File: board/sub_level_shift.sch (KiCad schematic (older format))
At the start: 31 parts, among them Q1401 Q_NPN_BEC, Q1402 Q_NPN_BEC, Q1403 Q_NPN_BEC, U1401 74LVC4245A, U1402 74LVC4245A, U1403 74LVC4245A, U1404 74LVC4245A, U1405 74LVC4245A, U1406 74LVC4245A, U1407 74LVC4245A

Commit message: Most footprints associated
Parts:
- C1401, C1402, C1403, C1404, C1405, C1406, C1407, C1408, C1409, C1410, C1411, C1412, C1413, C1414: footprint (none) -> Capacitor_SMD:C_0603_1608Metric
- Q1401, Q1402, Q1403: footprint (none) -> Package_TO_SOT_SMD:SOT-23
- R1401, R1402, R1403, R1404, R1405, R1406, R1407: footprint (none) -> Resistor_SMD:R_0603_1608Metric
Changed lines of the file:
@@
 F 0 "R1404" V 7418 4750 50  0000 C CNN
 F 1 "1k" V 7509 4750 50  0000 C CNN
-F 2 "" V 7555 4750 50  0001 C CNN
+F 2 "Resistor_SMD:R_0603_1608Metric" V 7555 4750 50  0001 C CNN
 F 3 "~" H 7625 4750 50  0001 C CNN
 	1    7625 4750
@@
 F 0 "Q1402" H 7466 4750 50  0000 L CNN
 F 1 "Q_NPN_BEC" H 7466 4705 50  0001 L CNN
-F 2 "" H 7475 4850 50  0001 C CNN
+F 2 "Package_TO_SOT_SMD:SOT-23" H 7475 4850 50  0001 C CNN
 F 3 "~" H 7275 4750 50  0001 C CNN
 	1    7275 4750
@@
 F 0 "R1403" H 6875 4350 50  0000 L CNN
 F 1 "4K7" H 6950 4250 50  0000 L CNN
-F 2 "" V 7105 4300 50  0001 C CNN
+F 2 "Resistor_SMD:R_0603_1608Metric" V 7105 4300 50  0001 C CNN
 F 3 "~" H 7175 4300 50  0001 C CNN
 	1    7175 4300
@@
 F 0 "R1407" H 6250 5900 50  0000 L CNN
 F 1 "4K7" H 6325 5800 50  0000 L CNN
-F 2 "" V 6480 5850 50  0001 C CNN
+F 2 "Resistor_SMD:R_0603_1608Metric" V 6480 5850 50  0001 C CNN
 F 3 "~" H 6550 5850 50  0001 C CNN
 	1    6550 5850
@@
 F 0 "R1402" V 8293 3775 50  0000 C CNN
 F 1 "1k" V 8384 3775 50  0000 C CNN
-F 2 "" V 8430 3775 50  0001 C CNN
+F 2 "Resistor_SMD:R_0603_1608Metric" V 8430 3775 50  0001 C CNN
 F 3 "~" H 8500 3775 50  0001 C CNN
 	1    8500 3775
@@
 F 0 "Q1401" H 8341 3775 50  0000 L CNN
 F 1 "Q_NPN_BEC" H 8341 3730 50  0001 L CNN
-F 2 "" H 8350 3875 50  0001 C CNN
+F 2 "Package_TO_SOT_SMD:SOT-23" H 8350 3875 50  0001 C CNN
 F 3 "~" H 8150 3775 50  0001 C CNN
 	1    8150 3775
@@
 F 0 "R1401" H 7750 3375 50  0000 L CNN
 F 1 "4K7" H 7825 3275 50  0000 L CNN
-F 2 "" V 7980 3325 50  0001 C CNN
+F 2 "Resistor_SMD:R_0603_1608Metric" V 7980 3325 50  0001 C CNN
 F 3 "~" H 8050 3325 50  0001 C CNN
 	1    8050 3325
@@
 F 0 "Q1403" H 8516 5550 50  0000 L CNN
 F 1 "Q_NPN_BEC" H 8516 5505 50  0001 L CNN
-F 2 "" H 8525 5650 50  0001 C CNN
+F 2 "Package_TO_SOT_SMD:SOT-23" H 8525 5650 50  0001 C CNN
 F 3 "~" H 8325 5550 50  0001 C CNN
 	1    8325 5550
@@
 F 0 "R1405" H 8500 5150 50  0000 L CNN
 F 1 "4K7" H 8500 5050 50  0000 L CNN
-F 2 "" V 8355 5100 50  0001 C CNN
+F 2 "Resistor_SMD:R_0603_1608Metric" V 8355 5100 50  0001 C CNN
 F 3 "~" H 8425 5100 50  0001 C CNN
 	1    8425 5100
@@
 F 0 "R1406" V 7775 5425 50  0000 L CNN
 F 1 "4K7" V 7875 5475 50  0000 L CNN
-F 2 "" V 7905 5550 50  0001 C CNN
+F 2 "Resistor_SMD:R_0603_1608Metric" V 7905 5550 50  0001 C CNN
 F 3 "~" H 7975 5550 50  0001 C CNN
 	1    7975 5550
@@
 F 0 "C1404" H 9715 2021 50  0000 L CNN
 F 1 "1u" H 9715 1930 50  0000 L CNN
-F 2 "" H 9638 1825 50  0001 C CNN
+F 2 "Capacitor_SMD:C_0603_1608Metric" H 9638 1825 50  0001 C CNN
 F 3 "~" H 9600 1975 50  0001 C CNN
 	1    9600 1975
@@
 F 0 "C1405" H 10190 2021 50  0000 L CNN
 F 1 "1u" H 10190 1930 50  0000 L CNN
-F 2 "" H 10113 1825 50  0001 C CNN
+F 2 "Capacitor_SMD:C_0603_1608Metric" H 10113 1825 50  0001 C CNN
 F 3 "~" H 10075 1975 50  0001 C CNN
 	1    10075 1975
@@
 F 0 "C1406" H 9715 2846 50  0000 L CNN
 F 1 "1u" H 9715 2755 50  0000 L CNN
-F 2 "" H 9638 2650 50  0001 C CNN
+F 2 "Capacitor_SMD:C_0603_1608Metric" H 9638 2650 50  0001 C CNN
 F 3 "~" H 9600 2800 50  0001 C CNN
 	1    9600 2800
@@
 F 0 "C1407" H 10190 2846 50  0000 L CNN
 F 1 "1u" H 10190 2755 50  0000 L CNN
-F 2 "" H 10113 2650 50  0001 C CNN
+F 2 "Capacitor_SMD:C_0603_1608Metric" H 10113 2650 50  0001 C CNN
 F 3 "~" H 10075 2800 50  0001 C CNN
 	1    10075 2800
@@
 F 0 "C1401" H 9715 1196 50  0000 L CNN
 F 1 "1u" H 9715 1105 50  0000 L CNN
-F 2 "" H 9638 1000 50  0001 C CNN
+F 2 "Capacitor_SMD:C_0603_1608Metric" H 9638 1000 50  0001 C CNN
 F 3 "~" H 9600 1150 50  0001 C CNN
 	1    9600 1150
@@
 F 0 "C1402" H 10190 1196 50  0000 L CNN
 F 1 "1u" H 10190 1105 50  0000 L CNN
-F 2 "" H 10113 1000 50  0001 C CNN
+F 2 "Capacitor_SMD:C_0603_1608Metric" H 10113 1000 50  0001 C CNN
 F 3 "~" H 10075 1150 50  0001 C CNN
 	1    10075 1150
@@
 F 0 "C1403" H 10665 1196 50  0000 L CNN
 F 1 "1u" H 10665 1105 50  0000 L CNN
-F 2 "" H 10588 1000 50  0001 C CNN
+F 2 "Capacitor_SMD:C_0603_1608Metric" H 10588 1000 50  0001 C CNN
 F 3 "~" H 10550 1150 50  0001 C CNN
 	1    10550 1150
@@
 F 0 "C1411" H 9715 4896 50  0000 L CNN
 F 1 "1u" H 9715 4805 50  0000 L CNN
-F 2 "" H 9638 4700 50  0001 C CNN
+F 2 "Capacitor_SMD:C_0603_1608Metric" H 9638 4700 50  0001 C CNN
 F 3 "~" H 9600 4850 50  0001 C CNN
 	1    9600 4850
@@
 F 0 "C1412" H 10190 4896 50  0000 L CNN
 F 1 "1u" H 10190 4805 50  0000 L CNN
-F 2 "" H 10113 4700 50  0001 C CNN
+F 2 "Capacitor_SMD:C_0603_1608Metric" H 10113 4700 50  0001 C CNN
 F 3 "~" H 10075 4850 50  0001 C CNN
 	1    10075 4850
@@
 F 0 "C1413" H 9715 5721 50  0000 L CNN
 F 1 "1u" H 9715 5630 50  0000 L CNN
-F 2 "" H 9638 5525 50  0001 C CNN
+F 2 "Capacitor_SMD:C_0603_1608Metric" H 9638 5525 50  0001 C CNN
 F 3 "~" H 9600 5675 50  0001 C CNN
 	1    9600 5675
@@
 F 0 "C1414" H 10190 5721 50  0000 L CNN
 F 1 "1u" H 10190 5630 50  0000 L CNN
-F 2 "" H 10113 5525 50  0001 C CNN
+F 2 "Capacitor_SMD:C_0603_1608Metric" H 10113 5525 50  0001 C CNN
 F 3 "~" H 10075 5675 50  0001 C CNN
 	1    10075 5675
@@
 F 0 "C1408" H 9715 4071 50  0000 L CNN
 F 1 "1u" H 9715 3980 50  0000 L CNN
-F 2 "" H 9638 3875 50  0001 C CNN
+F 2 "Capacitor_SMD:C_0603_1608Metric" H 9638 3875 50  0001 C CNN
 F 3 "~" H 9600 4025 50  0001 C CNN
 	1    9600 4025
@@
 F 0 "C1409" H 10190 4071 50  0000 L CNN
 F 1 "1u" H 10190 3980 50  0000 L CNN
-F 2 "" H 10113 3875 50  0001 C CNN
+F 2 "Capacitor_SMD:C_0603_1608Metric" H 10113 3875 50  0001 C CNN
 F 3 "~" H 10075 4025 50  0001 C CNN
 	1    10075 4025
@@
 F 0 "C1410" H 10665 4071 50  0000 L CNN
 F 1 "1u" H 10665 3980 50  0000 L CNN
-F 2 "" H 10588 3875 50  0001 C CNN
+F 2 "Capacitor_SMD:C_0603_1608Metric" H 10588 3875 50  0001 C CNN
 F 3 "~" H 10550 4025 50  0001 C CNN
 	1    10550 4025

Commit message: Started on board
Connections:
- net GND: now also U1405.14 (B7)
- no-connect marks 14 -> 13
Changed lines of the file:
@@
 Text Label 4300 4700 3    50   ~ 0
 5_A[19..16]
-NoConn ~ 5650 3950
 NoConn ~ 4600 3950
 $Comp
@@
 Text HLabel 4600 2350 3    50   Input ~ 0
 ~EnableXcvrs
+$Comp
+L power:GND #PWR?
+U 1 1 5AB2F0F1
+P 5700 4000
+F 0 "#PWR?" H 5700 3750 50  0001 C CNN
+F 1 "GND" H 5705 3827 50  0000 C CNN
+F 2 "" H 5700 4000 50  0001 C CNN
+F 3 "" H 5700 4000 50  0001 C CNN
+	1    5700 4000
+	1    0    0    -1
+$EndComp
+Wire Wire Line
+	5700 4000 5700 3950
+Wire Wire Line
+	5700 3950 5650 3950
 Wire Bus Line
 	5950 4650 5950 5600

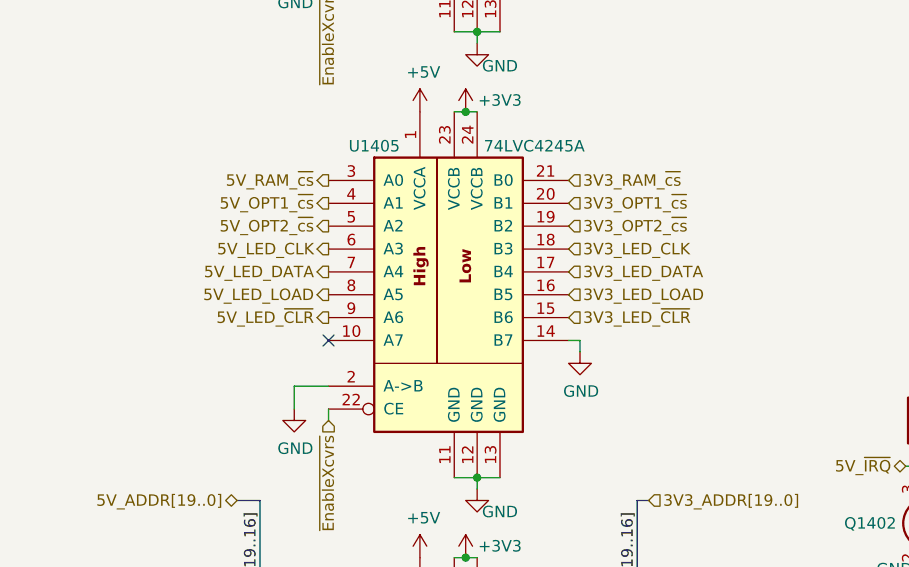
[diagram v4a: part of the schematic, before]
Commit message: Power supply routed
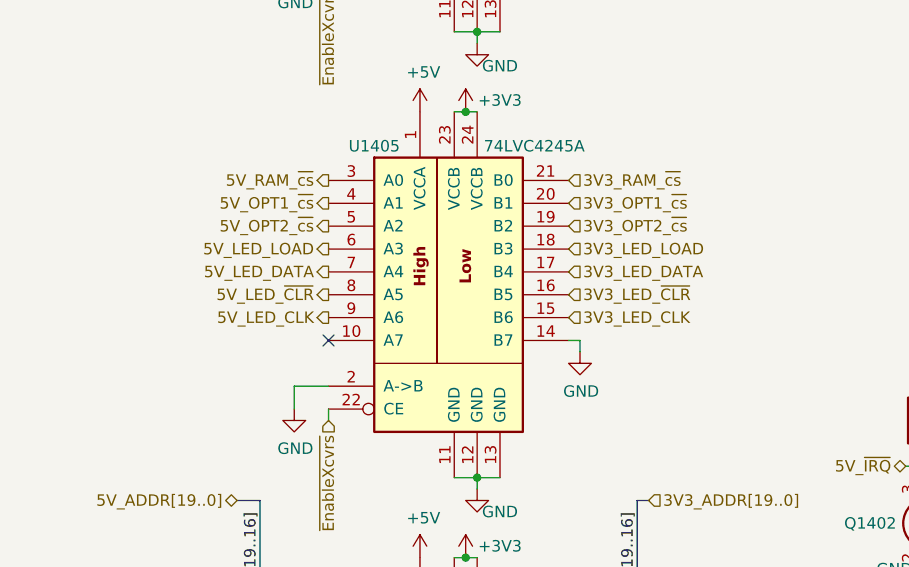
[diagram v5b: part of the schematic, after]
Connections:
- net 3V3_LED_CLK: now also U1405.15 (B6); no longer U1405.18 (B3)
- net 3V3_LED_LOAD: now also U1405.18 (B3); no longer U1405.16 (B5)
- net 3V3_LED_~CLR: now also U1405.16 (B5); no longer U1405.15 (B6)
- net 5V_LED_CLK: now also U1405.9 (A6); no longer U1405.6 (A3)
- net 5V_LED_LOAD: now also U1405.6 (A3); no longer U1405.8 (A5)
- net 5V_LED_~CLR: now also U1405.8 (A5); no longer U1405.9 (A6)
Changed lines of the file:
@@
 Wire Wire Line
 	4450 4150 4600 4150
-Text HLabel 4600 3550 0    50   Output ~ 0
+Text HLabel 4600 3850 0    50   Output ~ 0
 5V_LED_CLK
 Text HLabel 4600 3650 0    50   Output ~ 0
 5V_LED_DATA
-Text HLabel 4600 3750 0    50   Output ~ 0
+Text HLabel 4600 3550 0    50   Output ~ 0
 5V_LED_LOAD
 $Comp
@@
 Wire Wire Line
 	7250 2200 7350 2200
-Text HLabel 5650 3550 2    50   Input ~ 0
+Text HLabel 5650 3850 2    50   Input ~ 0
 3V3_LED_CLK
 Text HLabel 5650 3650 2    50   Input ~ 0
 3V3_LED_DATA
+Text HLabel 5650 3550 2    50   Input ~ 0
+3V3_LED_LOAD
 Text HLabel 5650 3750 2    50   Input ~ 0
-3V3_LED_LOAD
-Text HLabel 5650 3850 2    50   Input ~ 0
 3V3_LED_~CLR
-Text HLabel 4600 3850 0    50   Output ~ 0
+Text HLabel 4600 3750 0    50   Output ~ 0
 5V_LED_~CLR
 Wire Wire Line
@@
 ~EnableXcvrs
 $Comp
-L power:GND #PWR?
+L power:GND #PWR0101
 U 1 1 5AB2F0F1
 P 5700 4000
-F 0 "#PWR?" H 5700 3750 50  0001 C CNN
+F 0 "#PWR0101" H 5700 3750 50  0001 C CNN
 F 1 "GND" H 5705 3827 50  0000 C CNN
 F 2 "" H 5700 4000 50  0001 C CNN
